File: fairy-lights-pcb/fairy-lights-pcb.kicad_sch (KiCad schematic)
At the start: 19 parts, among them J1 Power_Jack, J2 Conn_LED_Strand_SPI, J3 Conn_LED_Strand_WS2812, J4 Conn_I2C, J5 Conn_02x04_Top_Bottom, SW1 SW_PWR, SW2 USER_A, SW3 USER_B, U1 WeMos_D1_mini

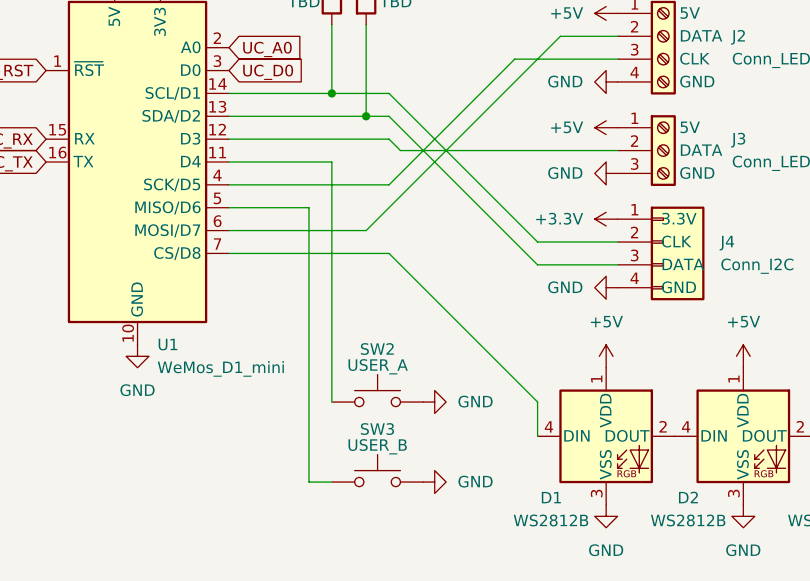
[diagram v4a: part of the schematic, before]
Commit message: Ground the mounting pins of the buttons
Also tweaks the location of the "5V 2A" label.
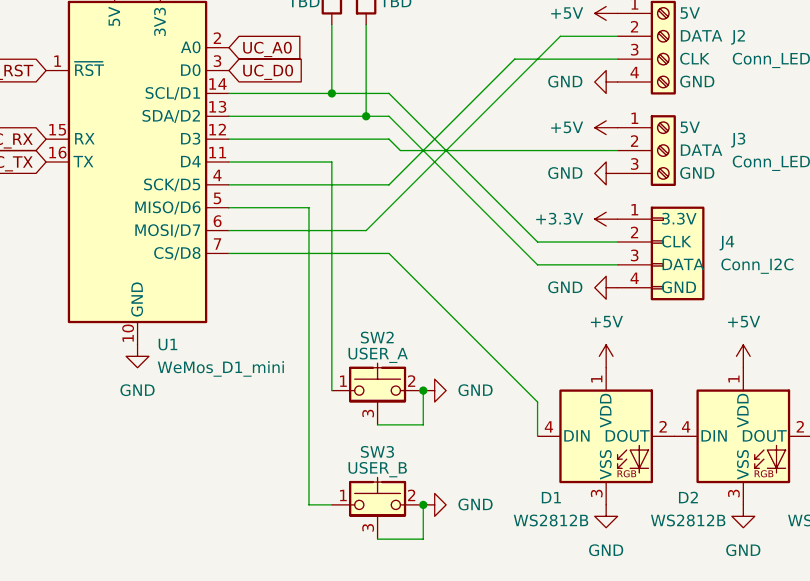
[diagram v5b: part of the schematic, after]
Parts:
- SW2, SW3: footprint Button_Switch_THT:SW_Tactile_SPST_Angled_PTS645Vx31-2LFS -> CustomLibrary:SW_Tactile_SPST_Angled_PTS645Vx31-2LFS_2MP; symbol Switch:SW_Push -> CustomSymbols:SW_Push_Shielded_2MP
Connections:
- net GND: now also SW2.3 (SH1), SW2.4 (SH2), SW3.3 (SH1), SW3.4 (SH2)
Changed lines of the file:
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@@
 	)
 	(junction
+		(at 146.05 114.3)
+		(diameter 0)
+		(color 0 0 0 0)
+	)
+	(junction
+		(at 146.05 101.6)
+		(diameter 0)
+		(color 0 0 0 0)
+	)
+	(junction
 		(at 139.7 71.12)
 		(diameter 0)
@@
 	(wire
 		(pts
+			(xy 140.97 105.41) (xy 146.05 105.41)
+		)
+		(stroke
+			(width 0)
+			(type default)
+		)
+	)
+	(wire
+		(pts
+			(xy 146.05 114.3) (xy 146.05 118.11)
+		)
+		(stroke
+			(width 0)
+			(type default)
+		)
+	)
+	(wire
+		(pts
 			(xy 135.89 53.34) (xy 139.7 53.34)
 		)
@@
 	(wire
 		(pts
-			(xy 133.35 111.76) (xy 135.89 111.76)
+			(xy 133.35 114.3) (xy 135.89 114.3)
 		)
 		(stroke
@@
 	(wire
 		(pts
-			(xy 135.89 76.2) (xy 135.89 102.87)
+			(xy 135.89 76.2) (xy 135.89 101.6)
+		)
+		(stroke
+			(width 0)
+			(type default)
+		)
+	)
+	(wire
+		(pts
+			(xy 140.97 118.11) (xy 146.05 118.11)
 		)
 		(stroke
@@
 	(wire
 		(pts
-			(xy 133.35 81.28) (xy 133.35 111.76)
+			(xy 133.35 81.28) (xy 133.35 114.3)
+		)
+		(stroke
+			(width 0)
+			(type default)
+		)
+	)
+	(wire
+		(pts
+			(xy 146.05 101.6) (xy 146.05 105.41)
 		)
 		(stroke
@@
 	)
 	(symbol
-		(lib_id "Switch:SW_Push")
-		(at 140.97 111.76 0)
+		(lib_id "CustomSymbols:SW_Push_Shielded_2MP")
+		(at 140.97 114.3 0)
 		(unit 1)
 		(exclude_from_sim no)
@@
 		(dnp no)
 		(property "Reference" "SW3"
-			(at 140.97 105.918 0)
+			(at 140.97 108.458 0)
 			(effects
 				(font
@@
 		)
 		(property "Value" "USER_B"
-			(at 140.97 107.696 0)
+			(at 140.97 110.236 0)
 			(effects
 				(font
@@
 			)
 		)
-		(property "Footprint" "Button_Switch_THT:SW_Tactile_SPST_Angled_PTS645Vx31-2LFS"
-			(at 140.97 106.68 0)
+		(property "Footprint" "CustomLibrary:SW_Tactile_SPST_Angled_PTS645Vx31-2LFS_2MP"
+			(at 140.97 109.22 0)
 			(effects
 				(font
@@
 		)
 		(property "Datasheet" "~"
-			(at 140.97 106.68 0)
+			(at 140.97 109.22 0)
 			(effects
 				(font
@@
 			)
 		)
-		(property "Description" "Push button switch, generic, two pins"
-			(at 140.97 111.76 0)
+		(property "Description" "Generic push-button switch, two contact pins and shield pin(s)"
+			(at 140.97 114.3 0)
 			(effects
 				(font
@@
 		(pin "1"
 		)
+		(pin "3"
+		)
+		(pin "4"
+		)
 		(instances
 			(project "fairy-lights-pcb"
@@
 	)
 	(symbol
-		(lib_id "Switch:SW_Push")
-		(at 140.97 102.87 0)
+		(lib_id "CustomSymbols:SW_Push_Shielded_2MP")
+		(at 140.97 101.6 0)
 		(unit 1)
 		(exclude_from_sim no)
@@
 		(dnp no)
 		(property "Reference" "SW2"
-			(at 140.97 97.028 0)
+			(at 140.97 95.758 0)
 			(effects
 				(font
@@
 		)
 		(property "Value" "USER_A"
-			(at 140.97 98.806 0)
+			(at 140.97 97.536 0)
 			(effects
 				(font
@@
 			)
 		)
-		(property "Footprint" "Button_Switch_THT:SW_Tactile_SPST_Angled_PTS645Vx31-2LFS"
-			(at 140.97 97.79 0)
+		(property "Footprint" "CustomLibrary:SW_Tactile_SPST_Angled_PTS645Vx31-2LFS_2MP"
+			(at 140.97 96.52 0)
 			(effects
 				(font
@@
 		)
 		(property "Datasheet" "~"
-			(at 140.97 97.79 0)
+			(at 140.97 96.52 0)
 			(effects
 				(font
@@
 			)
 		)
-		(property "Description" "Push button switch, generic, two pins"
-			(at 140.97 102.87 0)
+		(property "Description" "Generic push-button switch, two contact pins and shield pin(s)"
+			(at 140.97 101.6 0)
 			(effects
 				(font
@@
 		(pin "1"
 		)
+		(pin "4"
+		)
+		(pin "3"
+		)
 		(instances
 			(project ""
@@
 	(symbol
 		(lib_id "power:GND")
-		(at 146.05 102.87 90)
+		(at 146.05 101.6 90)
 		(unit 1)
 		(exclude_from_sim no)
@@
 		(fields_autoplaced yes)
 		(property "Reference" "#PWR018"
-			(at 152.4 102.87 0)
+			(at 152.4 101.6 0)
 			(effects
 				(font
@@
 		)
 		(property "Value" "GND"
-			(at 149.86 102.8699 90)
+			(at 149.86 101.5999 90)
 			(effects
 				(font
@@
 		)
 		(property "Footprint" ""
-			(at 146.05 102.87 0)
+			(at 146.05 101.6 0)
 			(effects
 				(font
@@
 		)
 		(property "Datasheet" ""
-			(at 146.05 102.87 0)
+			(at 146.05 101.6 0)
 			(effects
 				(font
@@
 		)
 		(property "Description" "Power symbol creates a global label with name \"GND\" , ground"
-			(at 146.05 102.87 0)
+			(at 146.05 101.6 0)
 			(effects
 				(font
@@
 	(symbol
 		(lib_id "power:GND")
-		(at 146.05 111.76 90)
+		(at 146.05 114.3 90)
 		(unit 1)
 		(exclude_from_sim no)
@@
 		(fields_autoplaced yes)
 		(property "Reference" "#PWR07"
-			(at 152.4 111.76 0)
+			(at 152.4 114.3 0)
 			(effects
 				(font
@@
 		)
 		(property "Value" "GND"
-			(at 149.86 111.7599 90)
+			(at 149.86 114.2999 90)
 			(effects
 				(font
@@
 		)
 		(property "Footprint" ""
-			(at 146.05 111.76 0)
+			(at 146.05 114.3 0)
 			(effects
 				(font
@@
 		)
 		(property "Datasheet" ""
-			(at 146.05 111.76 0)
+			(at 146.05 114.3 0)
 			(effects
 				(font
@@
 		)
 		(property "Description" "Power symbol creates a global label with name \"GND\" , ground"
-			(at 146.05 111.76 0)
+			(at 146.05 114.3 0)
 			(effects
 				(font

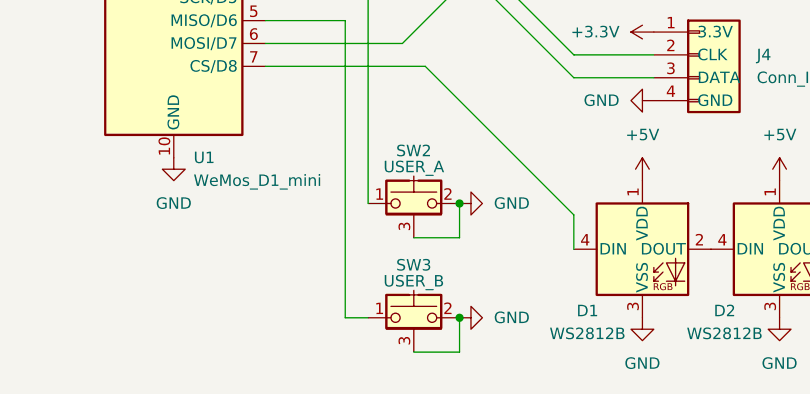
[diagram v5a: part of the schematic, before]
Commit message: Tweak push button footprint
Oh, hey, one can assign multiple footprint pads to the same schematic
pin!
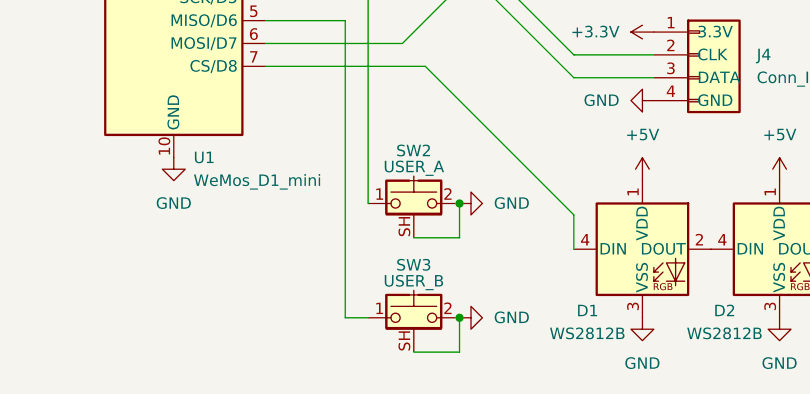
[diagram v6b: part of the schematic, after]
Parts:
- SW2, SW3: footprint CustomLibrary:SW_Tactile_SPST_Angled_PTS645Vx31-2LFS_2MP -> CustomLibrary:SW_Tactile_SPST_Angled_PTS645Vx31-2LFS_SH; symbol CustomSymbols:SW_Push_Shielded_2MP -> Switch:SW_Push_Shielded
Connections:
- net GND: now also SW2.SH (B), SW3.SH (B); no longer SW2.3 (SH1), SW2.4 (SH2), SW3.3 (SH1), SW3.4 (SH2)
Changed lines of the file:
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@@
 	)
 	(symbol
-		(lib_id "CustomSymbols:SW_Push_Shielded_2MP")
+		(lib_id "Switch:SW_Push_Shielded")
 		(at 140.97 114.3 0)
 		(unit 1)
@@
 			)
 		)
-		(property "Footprint" "CustomLibrary:SW_Tactile_SPST_Angled_PTS645Vx31-2LFS_2MP"
+		(property "Footprint" "CustomLibrary:SW_Tactile_SPST_Angled_PTS645Vx31-2LFS_SH"
 			(at 140.97 109.22 0)
 			(effects
@@
 		(pin "1"
 		)
-		(pin "3"
-		)
-		(pin "4"
+		(pin "SH"
 		)
 		(instances
@@
 	)
 	(symbol
-		(lib_id "CustomSymbols:SW_Push_Shielded_2MP")
+		(lib_id "Switch:SW_Push_Shielded")
 		(at 140.97 101.6 0)
 		(unit 1)
@@
 			)
 		)
-		(property "Footprint" "CustomLibrary:SW_Tactile_SPST_Angled_PTS645Vx31-2LFS_2MP"
+		(property "Footprint" "CustomLibrary:SW_Tactile_SPST_Angled_PTS645Vx31-2LFS_SH"
 			(at 140.97 96.52 0)
 			(effects
@@
 		(pin "1"
 		)
-		(pin "4"
-		)
-		(pin "3"
-		)
-		(instances
+		(pin "SH"
+		)
+		(instances

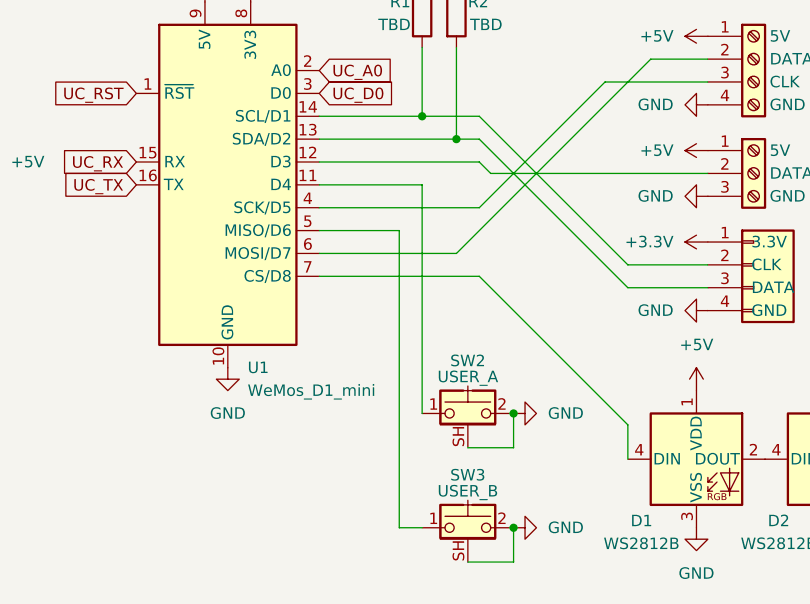
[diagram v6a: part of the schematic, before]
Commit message: Tweak MCU pin assignment
- Swaps the J3_DATA and USER_B pins.
- Now, all LED strand terminals and the I2C header are connected to GPIO
  pins with no strings (or, more accurately, random components on the
  MCU module) attached.
- Button USER_B puts the MCU flash mode if pressed at boot-up. The same
  can be achieved via USB, but, I guess, it's useful for flashing in the
  field with no USB but a UART?
- Button USER_A is tied to the same pin that drives the MCU module's
  on-board LED. When USER_A is pressed, the LED lights up. It might be
  worthwhile to re-wire USER_A to MCU pin D0 in order to free the LED
  and allow using USER_A as a soft power button (although that would
  require regularly polling the button in software while the MCU is
  running).
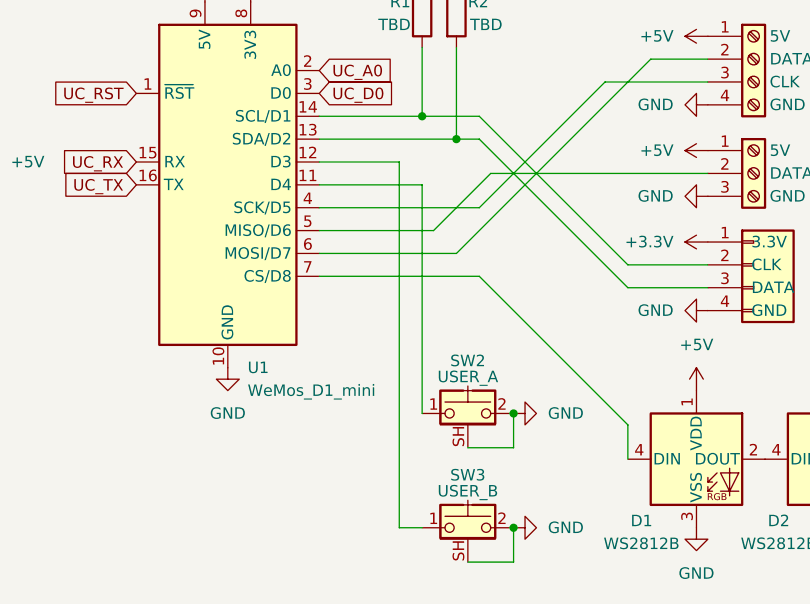
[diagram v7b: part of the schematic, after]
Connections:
- net at SW3.1: now also U1.12 (D3); no longer U1.5 (MISO/D6)
- net at J3.2 (DATA): now also U1.5 (MISO/D6); no longer U1.12 (D3)
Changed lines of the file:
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@@
+	(wire
+		(pts
+			(xy 133.35 73.66) (xy 133.35 114.3)
+		)
+		(stroke
+			(width 0)
+			(type default)
+		)
+	)
 	(wire
 		(pts
@@
 	(wire
 		(pts
-			(xy 124.46 81.28) (xy 133.35 81.28)
-		)
-		(stroke
-			(width 0)
-			(type default)
-		)
-	)
-	(wire
-		(pts
 			(xy 135.89 60.96) (xy 135.89 68.58)
 		)
@@
 	(wire
 		(pts
+			(xy 124.46 78.74) (xy 142.24 78.74)
+		)
+		(stroke
+			(width 0)
+			(type default)
+		)
+	)
+	(wire
+		(pts
+			(xy 167.64 64.77) (xy 156.21 64.77)
+		)
+		(stroke
+			(width 0)
+			(type default)
+		)
+	)
+	(wire
+		(pts
+			(xy 58.42 73.66) (xy 71.12 73.66)
+		)
+		(stroke
+			(width 0)
+			(type default)
+		)
+	)
+	(wire
+		(pts
+			(xy 133.35 73.66) (xy 124.46 73.66)
+		)
+		(stroke
+			(width 0)
+			(type default)
+		)
+	)
+	(wire
+		(pts
+			(xy 142.24 68.58) (xy 158.75 85.09)
+		)
+		(stroke
+			(width 0)
+			(type default)
+		)
+	)
+	(wire
+		(pts
 			(xy 124.46 76.2) (xy 135.89 76.2)
 		)
@@
 	(wire
 		(pts
-			(xy 124.46 78.74) (xy 142.24 78.74)
-		)
-		(stroke
-			(width 0)
-			(type default)
-		)
-	)
-	(wire
-		(pts
-			(xy 167.64 64.77) (xy 156.21 64.77)
-		)
-		(stroke
-			(width 0)
-			(type default)
-		)
-	)
-	(wire
-		(pts
-			(xy 58.42 73.66) (xy 71.12 73.66)
-		)
-		(stroke
-			(width 0)
-			(type default)
-		)
-	)
-	(wire
-		(pts
-			(xy 142.24 68.58) (xy 158.75 85.09)
-		)
-		(stroke
-			(width 0)
-			(type default)
-		)
-	)
-	(wire
-		(pts
 			(xy 124.46 83.82) (xy 139.7 83.82)
 		)
@@
 	(wire
 		(pts
+			(xy 140.97 118.11) (xy 146.05 118.11)
+		)
+		(stroke
+			(width 0)
+			(type default)
+		)
+	)
+	(wire
+		(pts
+			(xy 124.46 68.58) (xy 135.89 68.58)
+		)
+		(stroke
+			(width 0)
+			(type default)
+		)
+	)
+	(wire
+		(pts
+			(xy 142.24 78.74) (xy 156.21 64.77)
+		)
+		(stroke
+			(width 0)
+			(type default)
+		)
+	)
+	(wire
+		(pts
+			(xy 124.46 81.28) (xy 137.16 81.28)
+		)
+		(stroke
+			(width 0)
+			(type default)
+		)
+	)
+	(wire
+		(pts
 			(xy 135.89 76.2) (xy 135.89 101.6)
 		)
@@
 	(wire
 		(pts
-			(xy 140.97 118.11) (xy 146.05 118.11)
-		)
-		(stroke
-			(width 0)
-			(type default)
-		)
-	)
-	(wire
-		(pts
-			(xy 124.46 68.58) (xy 135.89 68.58)
-		)
-		(stroke
-			(width 0)
-			(type default)
-		)
-	)
-	(wire
-		(pts
-			(xy 142.24 78.74) (xy 156.21 64.77)
-		)
-		(stroke
-			(width 0)
-			(type default)
-		)
-	)
-	(wire
-		(pts
-			(xy 124.46 73.66) (xy 142.24 73.66)
-		)
-		(stroke
-			(width 0)
-			(type default)
-		)
-	)
-	(wire
-		(pts
 			(xy 142.24 86.36) (xy 158.75 102.87)
 		)
@@
 	(wire
 		(pts
-			(xy 143.51 74.93) (xy 142.24 73.66)
-		)
-		(stroke
-			(width 0)
-			(type default)
-		)
-	)
-	(wire
-		(pts
 			(xy 143.51 74.93) (xy 167.64 74.93)
 		)
@@
 	(wire
 		(pts
-			(xy 133.35 81.28) (xy 133.35 114.3)
-		)
-		(stroke
+			(xy 143.51 74.93) (xy 137.16 81.28)
+		)
+		(stroke

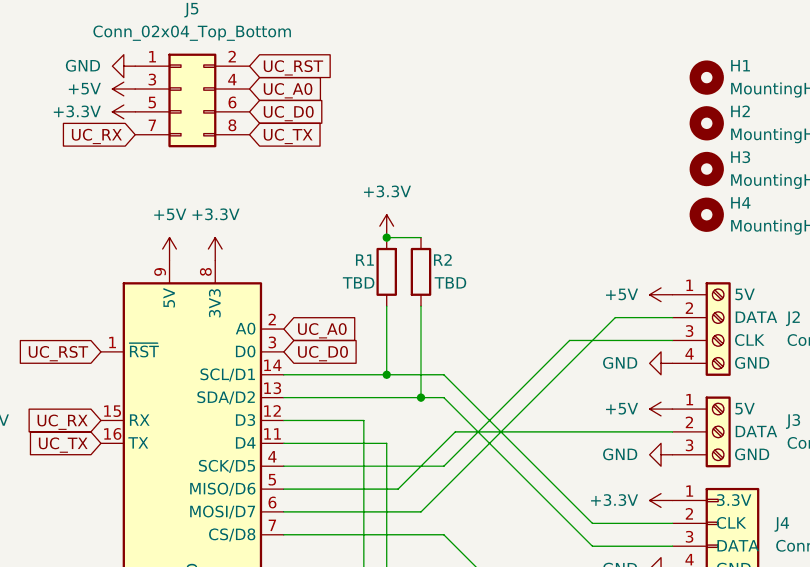
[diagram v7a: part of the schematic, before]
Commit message: Fix component labels and positions
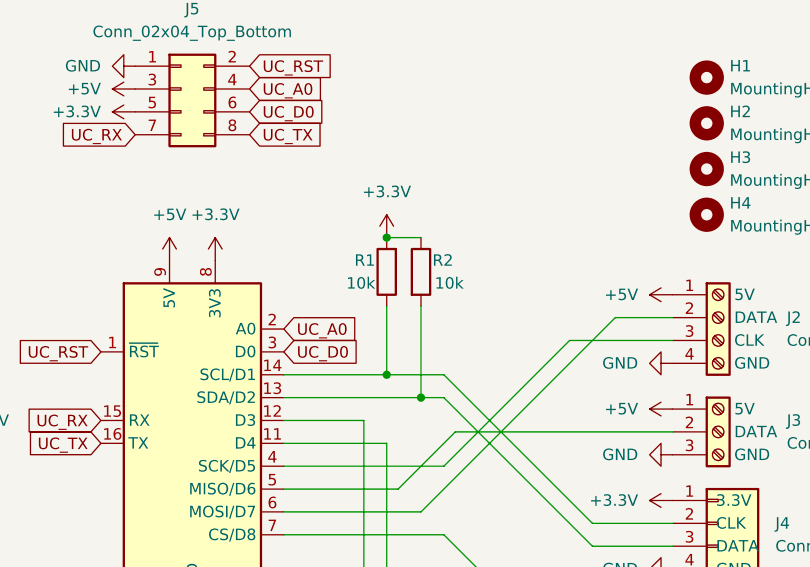
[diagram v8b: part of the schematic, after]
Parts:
- R1, R2: value TBD -> 10k
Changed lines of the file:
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@@
 			)
 		)
-		(property "Value" "TBD"
+		(property "Value" "10k"
 			(at 141.224 58.42 0)
 			(effects
@@
 			)
 		)
-		(property "Value" "TBD"
+		(property "Value" "10k"
 			(at 134.62 58.42 0)
 			(effects
